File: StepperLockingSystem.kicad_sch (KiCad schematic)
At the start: 21 parts, among them J1 Conn_01x01_Female, J2 Conn_01x01_Female, U1 TC1185, U2 SN65HVD232, U7 INA180A1

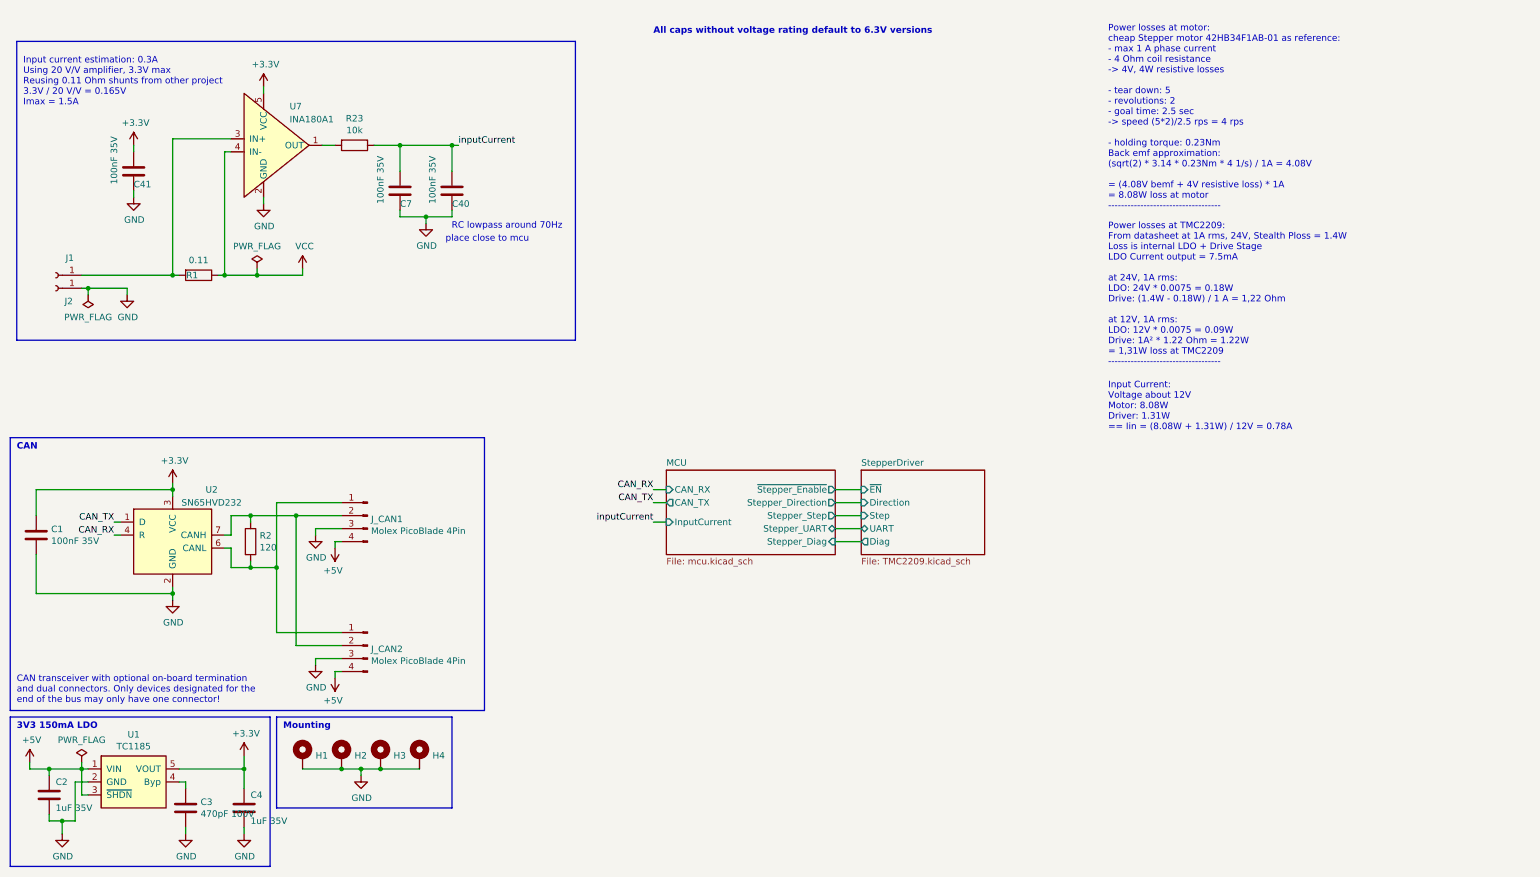
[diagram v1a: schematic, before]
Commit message: Rearrange schematic and some cleanups Add 5V buck converter Update values for TMC2209 Add EEPROM Switch to STM32G0B1KE
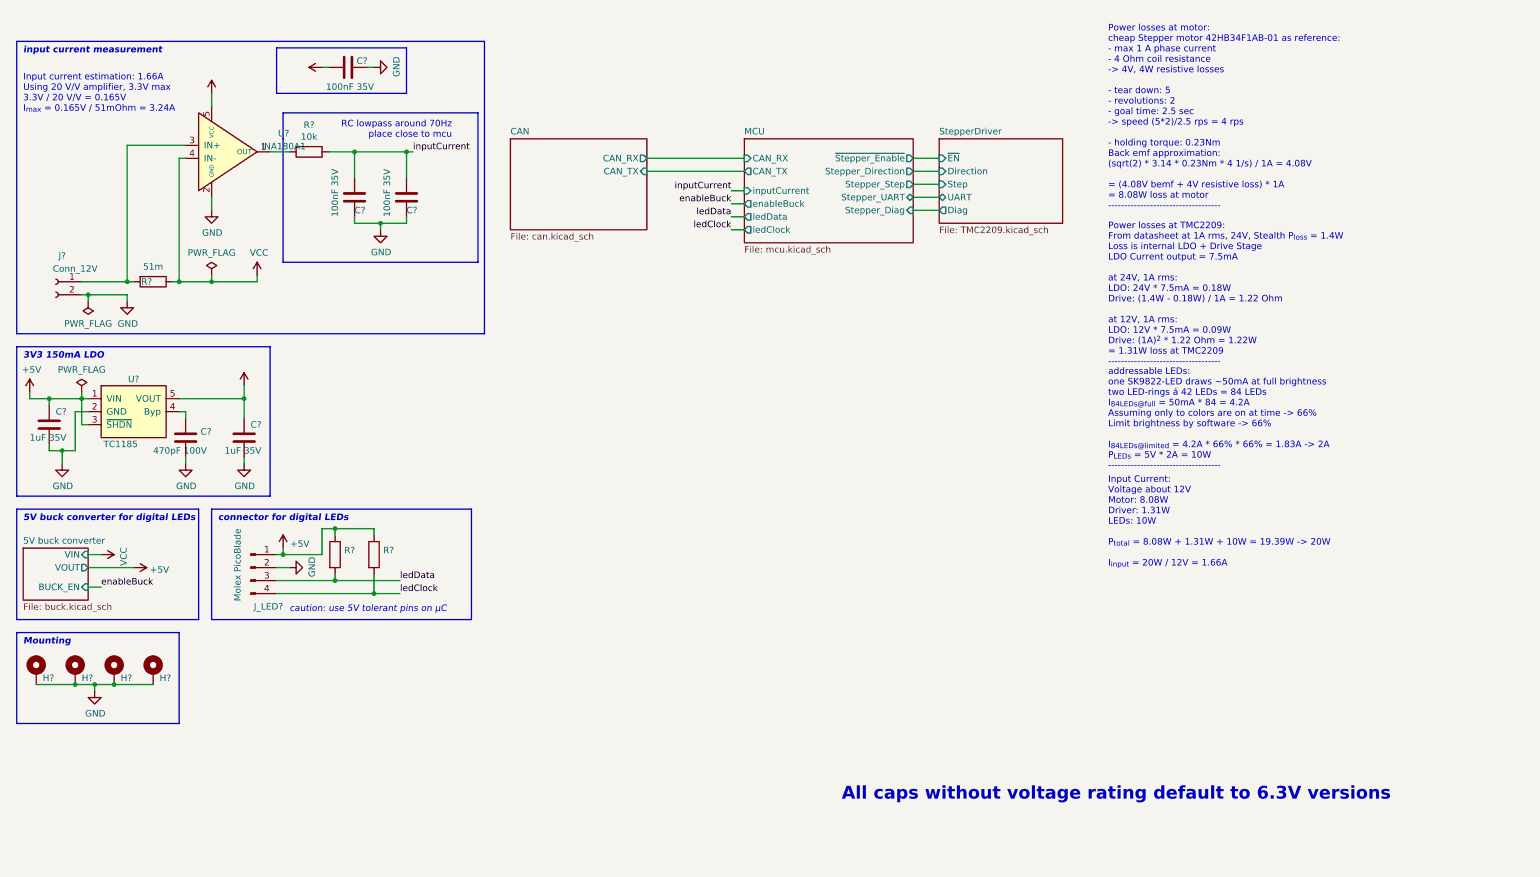
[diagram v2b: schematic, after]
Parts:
- removed C1: 100nF 35V, Capacitor_SMD:C_0603_1608Metric, symbol Device:C
- removed J1, J2: Conn_01x01_Female, TestPoint:TestPoint_Loop_D2.54mm_Drill1.5mm_Beaded, symbol Connector:Conn_01x01_Female
- removed J_CAN1, J_CAN2: Molex PicoBlade 4Pin, Connector_Molex:Molex_PicoBlade_53047-0410_1x04_P1.25mm_Vertical, symbol Connector:Conn_01x04_Male
- removed R2: 120, Resistor_SMD:R_0603_1608Metric, symbol Device:R
- removed U1: TC1185, Package_TO_SOT_SMD:SOT-23-5, symbol standardContent:TC1185
- removed U2: SN65HVD232, Package_SO:SOIC-8_3.9x4.9mm_P1.27mm, symbol Interface_CAN_LIN:SN65HVD232
- removed U7: INA180A1, Package_TO_SOT_SMD:SOT-23-5, symbol ti:INA180A1
- added J?: Conn_12V, symbol Connector:Conn_01x02_Female
- added J_LED?: Molex PicoBlade, Connector_Molex:Molex_PicoBlade_53047-0410_1x04_P1.25mm_Vertical, symbol Connector:Conn_01x04_Male
- added R? (x2): (no value), symbol Device:R
- added U?: TC1185, Package_TO_SOT_SMD:SOT-23-5, symbol extraSymbols:TC1185
- added U?: INA180A1, Package_TO_SOT_SMD:SOT-23-5, symbol extraSymbols:INA180A1
- R?: renamed from R1; value 0.11 -> 51m
- renumbered C2 to C?, C3 to C?, C4 to C?, C40 to C?, C7 to C?, C41 to C?, H1 to H?, H2 to H?, H3 to H?, H4 to H?, R23 to R?
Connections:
- net +3V3: now also U?.5 (VCC), U?.5 (VOUT)
- net +5V: now also J_LED?.1 (Pin_1), R?.1, R?.1, U?.1 (VIN), U?.3 (~{SHDN})
- net GND: now also J?.2 (Pin_2), J_LED?.2 (Pin_2), U?.2 (GND), U?.2 (GND)
- net VCC: now also U?.4 (IN-)
- net at C?.1: now also U?.4 (Byp)
- net at R?.2: now also J?.1 (Pin_1), U?.3 (IN+)
- net at R?.2: now also U?.1 (OUT)
- new net ledClock: J_LED?.4 (Pin_4), R?.2
- new net ledData: J_LED?.3 (Pin_3), R?.2
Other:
- added sheet 5V buck converter (buck.kicad_sch)
- added sheet CAN (can.kicad_sch)
- sheet MCU ports: added enableBuck, inputCurrent, ledClock, ledData; removed InputCurrent
- note added: "5V buck converter for digital LEDs"
- note added: "Input Current: Voltage about 12V Motor: 8.08W Driver: 1.31W LEDs: 10W P_{total} = 8.08W + 1.31W + 10W = 19.39W -> 20W I_{input} = 20W / 12V = 1.66A"
- note added: "Input current estimation: 1.66A Using 20 V/V amplifier, 3.3V max 3.3V / 20 V/V = 0.165V I_{max} = 0.165V / 51mOhm = 3.24A"
- note added: "Power losses at TMC2209: From datasheet at 1A rms, 24V, Stealth P_{loss} = 1.4W Loss is internal LDO + Drive Stage LDO Current output = 7.5mA at 24V, 1A rms: LDO: 24V * 7.5mA = 0.18W Drive: (1.4W - 0.18W) / 1A = 1.22 Ohm at 12V, 1A rms: LDO: 12V * 7.5mA = 0.09W Drive: (1A)^{2} * 1.22 Ohm = 1.22W = 1.31W loss at TMC2209 -----------------------------------"
- note added: "RC lowpass around 70Hz place close to mcu"
- note added: "addressable LEDs: one SK9822-LED draws ~50mA at full brightness two LED-rings á 42 LEDs = 84 LEDs I_{84LEDs@full} = 50mA * 84 = 4.2A Assuming only to colors are on at time -> 66% Limit brightness by software -> 66% I_{84LEDs@limited} = 4.2A * 66% * 66% = 1.83A -> 2A P_{LEDs} = 5V * 2A = 10W -----------------------------------"
- note added: "caution: use 5V tolerant pins on µC"
- note added: "connector for digital LEDs"
- note added: "input current measurement"
- note removed: "CAN"
- note removed: "CAN transceiver with optional on-board termination and dual connectors. Only devices designated for the end of the bus may only have one connector!"
- note removed: "Input Current: Voltage about 12V Motor: 8.08W Driver: 1.31W == Iin = (8.08W + 1.31W) / 12V = 0.78A"
- note removed: "Input current estimation: 0.3A Using 20 V/V amplifier, 3.3V max Reusing 0.11 Ohm shunts from other project 3.3V / 20 V/V = 0.165V Imax = 1.5A"
- note removed: "Power losses at TMC2209: From datasheet at 1A rms, 24V, Stealth Ploss = 1.4W Loss is internal LDO + Drive Stage LDO Current output = 7.5mA at 24V, 1A rms: LDO: 24V * 0.0075 = 0.18W Drive: (1.4W - 0.18W) / 1 A = 1,22 Ohm at 12V, 1A rms: LDO: 12V * 0.0075 = 0.09W Drive: 1A² * 1.22 Ohm = 1.22W = 1,31W loss at TMC2209 -----------------------------------"
- note removed: "RC lowpass around 70Hz"
- note removed: "place close to mcu"
- moved on the sheet: C?, H?, R?

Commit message: Small changes
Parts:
- R? (x2): value (none) -> 2k2
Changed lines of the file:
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@@
       (effects (font (size 1.27 1.27)) hide)
     )
-    (property "Value" "" (id 1) (at 59.69 80.2442 0))
+    (property "Value" "+3V3" (id 1) (at 59.69 80.2442 0))
     (property "Footprint" "" (id 2) (at 59.69 83.82 0)
       (effects (font (size 1.27 1.27)) hide)
@@
       (effects (font (size 1.27 1.27)) hide)
     )
-    (property "Value" "" (id 1) (at 53.34 23.0942 0))
+    (property "Value" "+3V3" (id 1) (at 53.34 23.0942 0))
     (property "Footprint" "" (id 2) (at 53.34 26.67 0)
       (effects (font (size 1.27 1.27)) hide)
@@
   )
   (symbol (lib_id "extraSymbols:INA180A1") (at 50.8 38.1 0) (unit 1)
-    (in_bom yes) (on_board yes) (fields_autoplaced)
-    (property "Reference" "U?" (id 0) (at 67.4196 34.4931 0))
-    (property "Value" "INA180A1" (id 1) (at 67.4196 37.03 0))
+    (in_bom yes) (on_board yes)
+    (property "Reference" "U?" (id 0) (at 58.42 33.02 0))
+    (property "Value" "INA180A1" (id 1) (at 60.96 43.18 0))
     (property "Footprint" "Package_TO_SOT_SMD:SOT-23-5" (id 2) (at 38.1 21.59 0)
       (effects (font (size 1.27 1.27)) hide)
@@
       (effects (font (size 1.27 1.27)) (justify left))
     )
-    (property "Value" "" (id 1) (at 79.248 118.5422 0)
+    (property "Value" "2k2" (id 1) (at 79.248 118.5422 0)
       (effects (font (size 1.27 1.27)) (justify left))
     )
@@
       (effects (font (size 1.27 1.27)) (justify left))
     )
-    (property "Value" "" (id 1) (at 86.868 118.5422 0)
+    (property "Value" "2k2" (id 1) (at 86.868 118.5422 0)
       (effects (font (size 1.27 1.27)) (justify left))
     )
@@
       (effects (font (size 1.27 1.27)) hide)
     )
-    (property "Value" "" (id 1) (at 71.755 22.0238 90)
+    (property "Value" "+3V3" (id 1) (at 71.755 22.0238 90)
       (effects (font (size 1.27 1.27)) (justify left))
     )
@@
     )
     (path "/00000000-0000-0000-0000-00005fd04053/b2db0251-456d-4632-b3df-e2ba1e27d44e"
-      (reference "C?") (unit 1) (value "~") (footprint "Capacitor_SMD:C_0603_1608Metric")
+      (reference "C?") (unit 1) (value "1u") (footprint "Capacitor_SMD:C_0603_1608Metric")
     )
     (path "/00000000-0000-0000-0000-00005fba2aff/b8e444d8-a839-4d88-8177-a5290090eb24"

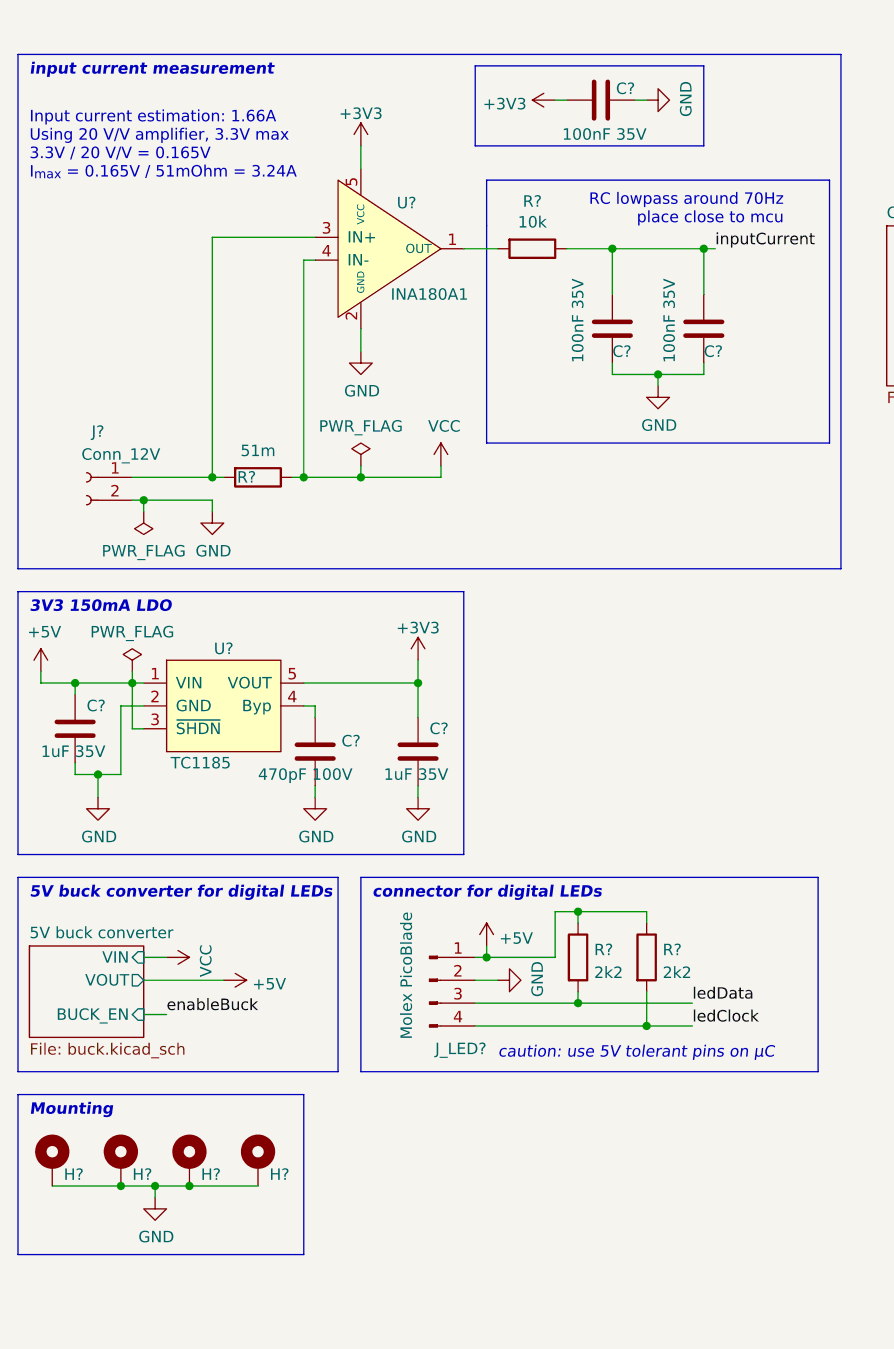
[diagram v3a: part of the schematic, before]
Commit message: Annotate symbols and assign footprints
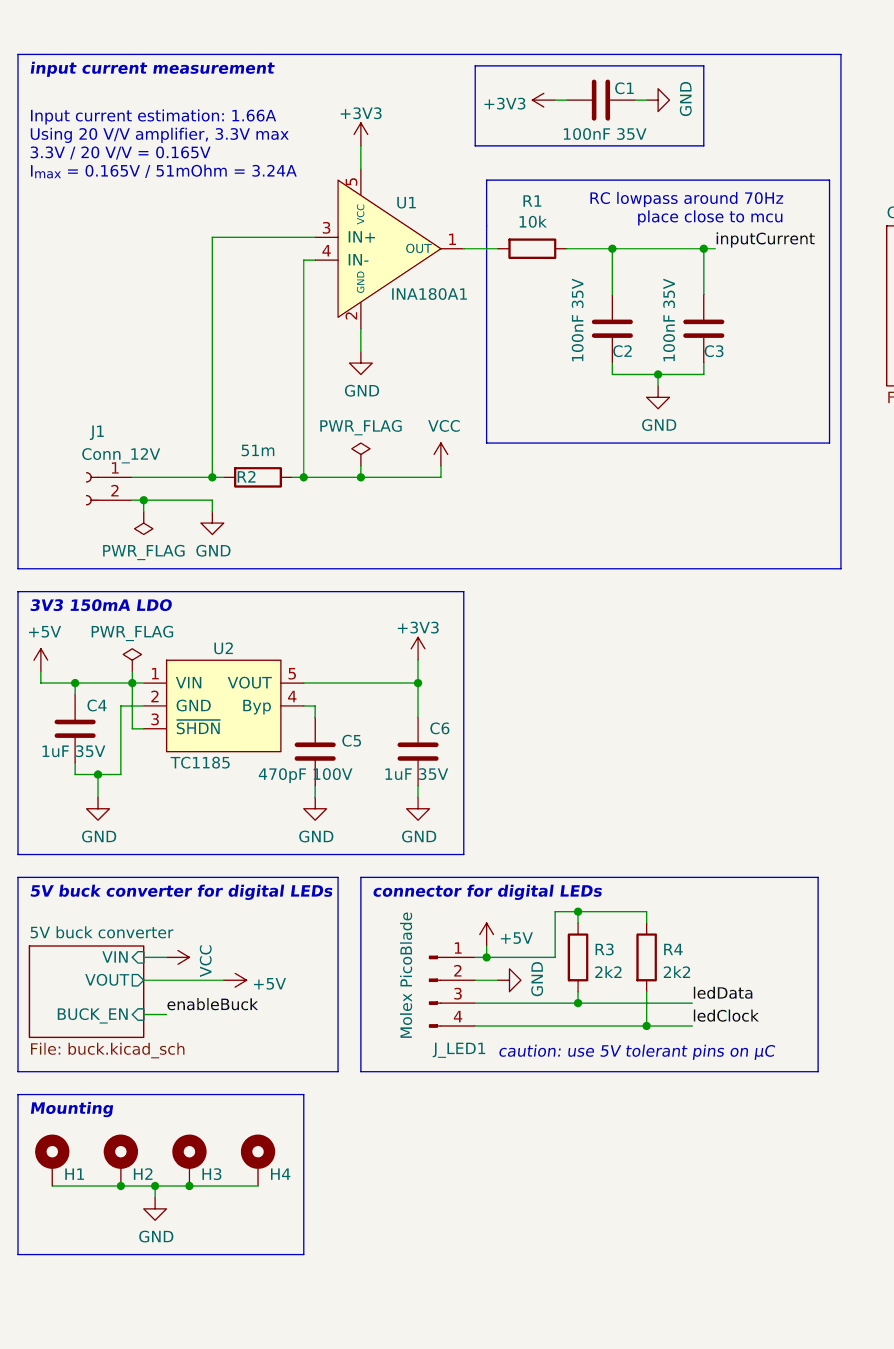
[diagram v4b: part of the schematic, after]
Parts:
- gave numbers to parts that had none: 18

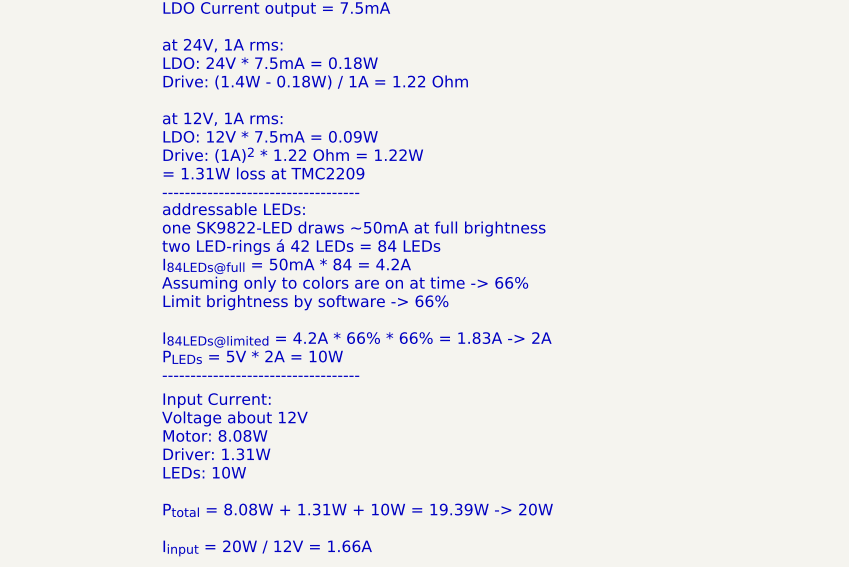
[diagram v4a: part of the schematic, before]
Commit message: Finish schematic
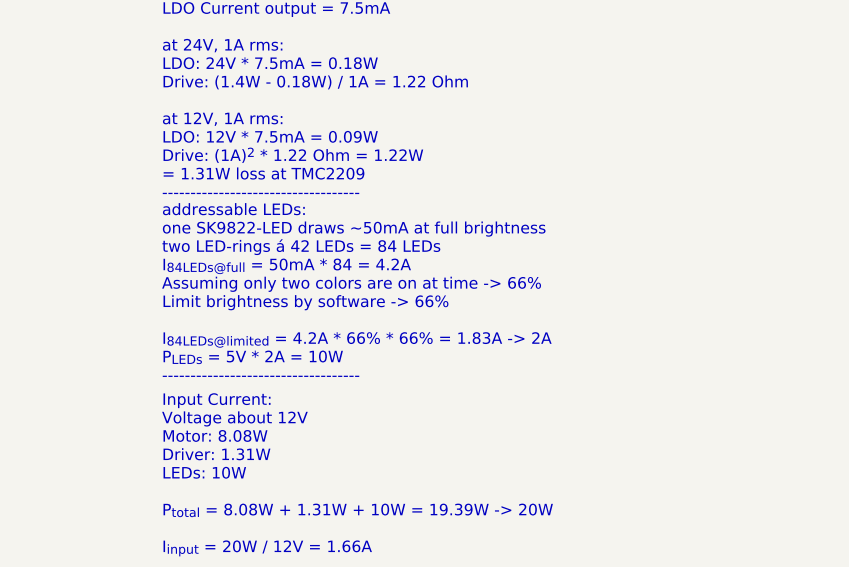
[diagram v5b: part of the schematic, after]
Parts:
- J1: footprint (none) -> Connector_AMASS:AMASS_XT30U-M_1x02_P5.0mm_Vertical
- R3, R4: footprint (none) -> Resistor_SMD:R_0603_1608Metric
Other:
- note added: "addressable LEDs: one SK9822-LED draws ~50mA at full brightness two LED-rings á 42 LEDs = 84 LEDs I_{84LEDs@full} = 50mA * 84 = 4.2A Assuming only two colors are on at time -> 66% Limit brightness by software -> 66% I_{84LEDs@limited} = 4.2A * 66% * 66% = 1.83A -> 2A P_{LEDs} = 5V * 2A = 10W -----------------------------------"
- note removed: "addressable LEDs: one SK9822-LED draws ~50mA at full brightness two LED-rings á 42 LEDs = 84 LEDs I_{84LEDs@full} = 50mA * 84 = 4.2A Assuming only to colors are on at time -> 66% Limit brightness by software -> 66% I_{84LEDs@limited} = 4.2A * 66% * 66% = 1.83A -> 2A P_{LEDs} = 5V * 2A = 10W -----------------------------------"
